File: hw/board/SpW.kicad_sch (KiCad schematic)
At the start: 8 parts

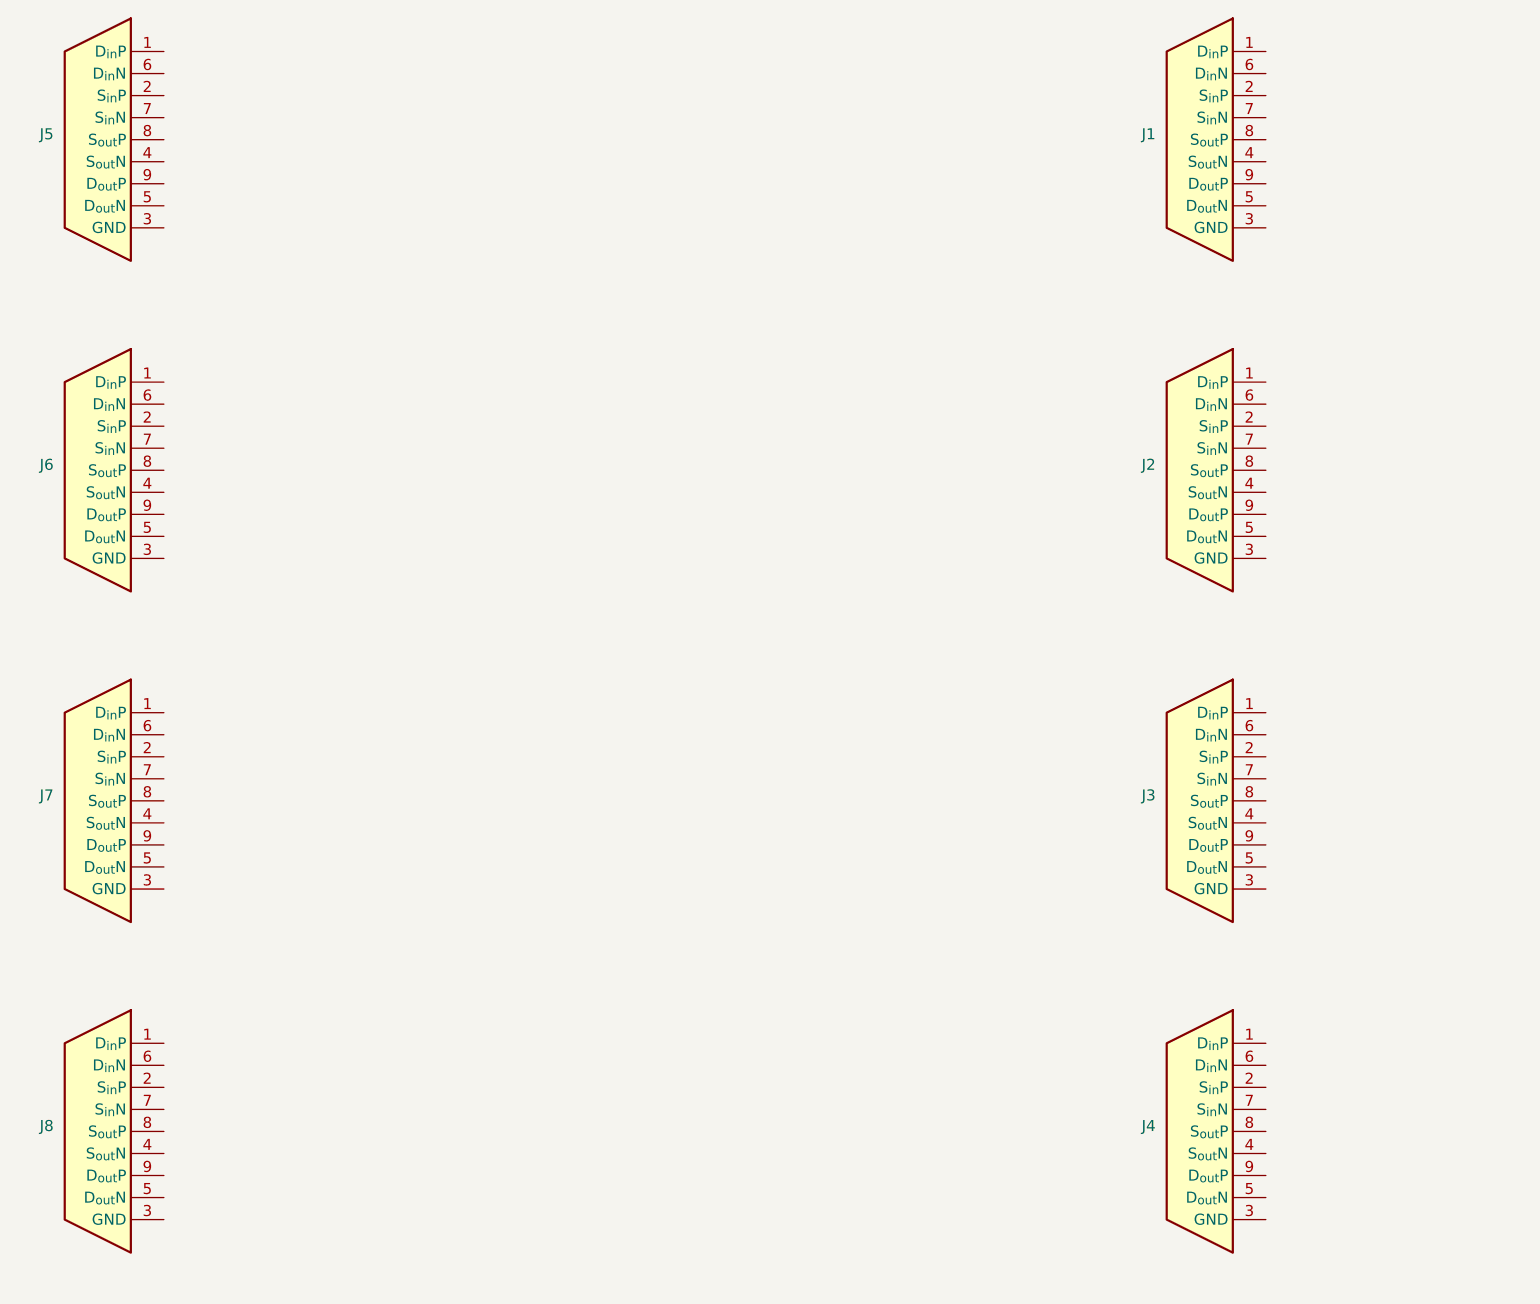
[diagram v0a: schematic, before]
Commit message: Routed DE-9 connectors
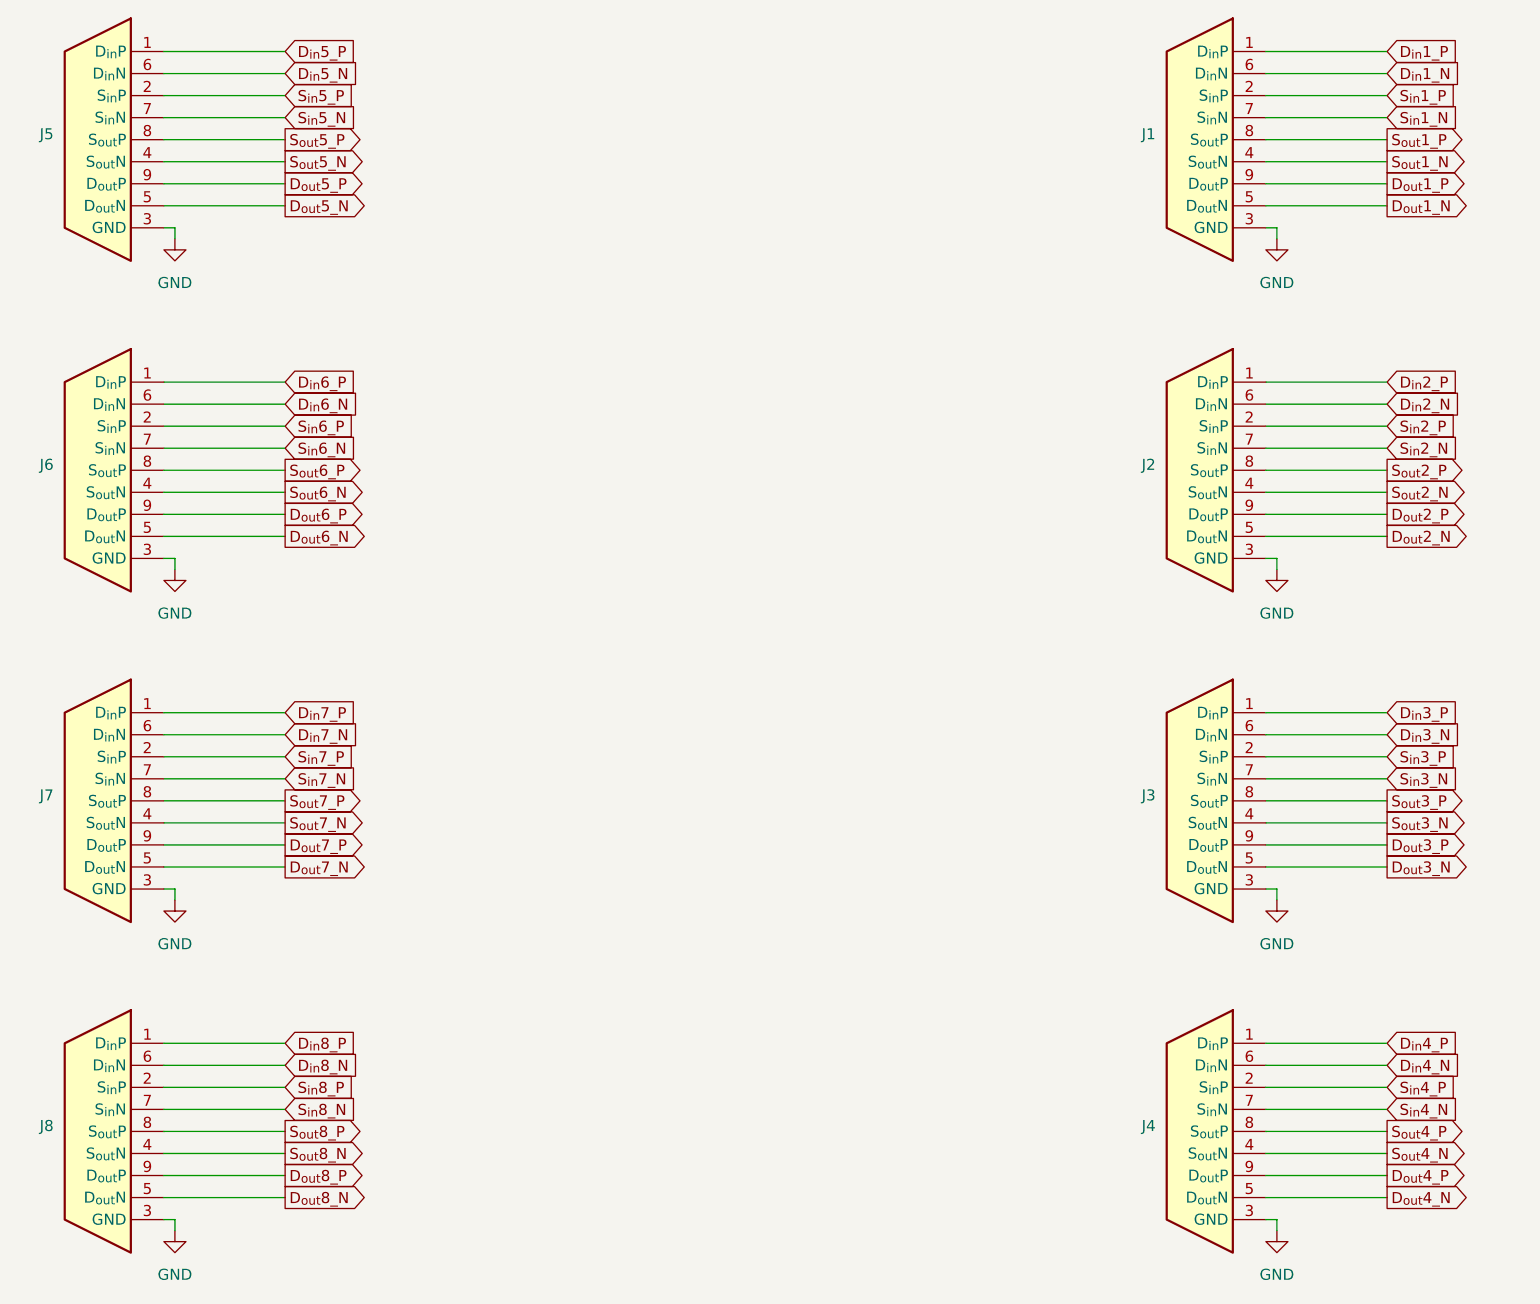
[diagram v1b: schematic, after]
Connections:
- net D_{in}3_P: now reaches J3.1 (D_{in}P)
- net S_{in}3_P: now reaches J3.2 (S_{in}P)
- net GND: now reaches J3.3 (GND)
- net GND: now also J1.3 (GND), J2.3 (GND), J4.3 (GND), J5.3 (GND), J6.3 (GND), J7.3 (GND), J8.3 (GND)
- net S_{out}3_N: now reaches J3.4 (S_{out}N)
- net D_{out}3_N: now reaches J3.5 (D_{out}N)
- net D_{in}3_N: now reaches J3.6 (D_{in}N)
- net S_{in}3_N: now reaches J3.7 (S_{in}N)
- net S_{out}3_P: now reaches J3.8 (S_{out}P)
- net D_{out}3_P: now reaches J3.9 (D_{out}P)
- net D_{in}1_P: now reaches J1.1 (D_{in}P)
- net S_{in}1_P: now reaches J1.2 (S_{in}P)
- net S_{out}1_N: now reaches J1.4 (S_{out}N)
- net D_{out}1_N: now reaches J1.5 (D_{out}N)
- net D_{in}1_N: now reaches J1.6 (D_{in}N)
- net S_{in}1_N: now reaches J1.7 (S_{in}N)
- net S_{out}1_P: now reaches J1.8 (S_{out}P)
- net D_{out}1_P: now reaches J1.9 (D_{out}P)
- net D_{in}4_P: now reaches J4.1 (D_{in}P)
- net S_{in}4_P: now reaches J4.2 (S_{in}P)
- net S_{out}4_N: now reaches J4.4 (S_{out}N)
- net D_{out}4_N: now reaches J4.5 (D_{out}N)
- net D_{in}4_N: now reaches J4.6 (D_{in}N)
- net S_{in}4_N: now reaches J4.7 (S_{in}N)
- net S_{out}4_P: now reaches J4.8 (S_{out}P)
- net D_{out}4_P: now reaches J4.9 (D_{out}P)
- net D_{in}6_P: now reaches J6.1 (D_{in}P)
- net S_{in}6_P: now reaches J6.2 (S_{in}P)
- net S_{out}6_N: now reaches J6.4 (S_{out}N)
- net D_{out}6_N: now reaches J6.5 (D_{out}N)
- net D_{in}6_N: now reaches J6.6 (D_{in}N)
- net S_{in}6_N: now reaches J6.7 (S_{in}N)
- net S_{out}6_P: now reaches J6.8 (S_{out}P)
- net D_{out}6_P: now reaches J6.9 (D_{out}P)
- net D_{in}2_P: now reaches J2.1 (D_{in}P)
- net S_{in}2_P: now reaches J2.2 (S_{in}P)
- net S_{out}2_N: now reaches J2.4 (S_{out}N)
- net D_{out}2_N: now reaches J2.5 (D_{out}N)
- net D_{in}2_N: now reaches J2.6 (D_{in}N)
- net S_{in}2_N: now reaches J2.7 (S_{in}N)
- net S_{out}2_P: now reaches J2.8 (S_{out}P)
- net D_{out}2_P: now reaches J2.9 (D_{out}P)
- net D_{in}7_P: now reaches J7.1 (D_{in}P)
- net S_{in}7_P: now reaches J7.2 (S_{in}P)
- net S_{out}7_N: now reaches J7.4 (S_{out}N)
- net D_{out}7_N: now reaches J7.5 (D_{out}N)
- net D_{in}7_N: now reaches J7.6 (D_{in}N)
- net S_{in}7_N: now reaches J7.7 (S_{in}N)
- net S_{out}7_P: now reaches J7.8 (S_{out}P)
- net D_{out}7_P: now reaches J7.9 (D_{out}P)
- net D_{in}8_P: now reaches J8.1 (D_{in}P)
- net S_{in}8_P: now reaches J8.2 (S_{in}P)
- net S_{out}8_N: now reaches J8.4 (S_{out}N)
- net D_{out}8_N: now reaches J8.5 (D_{out}N)
- net D_{in}8_N: now reaches J8.6 (D_{in}N)
- net S_{in}8_N: now reaches J8.7 (S_{in}N)
- net S_{out}8_P: now reaches J8.8 (S_{out}P)
- net D_{out}8_P: now reaches J8.9 (D_{out}P)
- net D_{in}5_P: now reaches J5.1 (D_{in}P)
- net S_{in}5_P: now reaches J5.2 (S_{in}P)
- net S_{out}5_N: now reaches J5.4 (S_{out}N)
- net D_{out}5_N: now reaches J5.5 (D_{out}N)
- net D_{in}5_N: now reaches J5.6 (D_{in}N)
- net S_{in}5_N: now reaches J5.7 (S_{in}N)
- net S_{out}5_P: now reaches J5.8 (S_{out}P)
- net D_{out}5_P: now reaches J5.9 (D_{out}P)

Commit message: Reannotated piece numbers
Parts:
- renumbered J7 to J10, J2 to J3, J3 to J4, J6 to J5, J8 to J6, J1 to J7, J4 to J8, J5 to J9
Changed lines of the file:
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@@
 		(dnp no)
 		(fields_autoplaced yes)
-		(property "Reference" "J3"
+		(property "Reference" "J4"
 			(at 151.13 111.1249 0)
 			(effects
@@
 			(project "board"
 				(path "/0e384709-6bce-4dbf-a0e0-550e970390f4/3792d272-ff69-4aa2-a357-018752cd6a75"
-					(reference "J3")
+					(reference "J4")
 					(unit 1)
 				)
@@
 		(dnp no)
 		(fields_autoplaced yes)
-		(property "Reference" "J1"
+		(property "Reference" "J7"
 			(at 151.13 34.9249 0)
 			(effects
@@
 			(project "board"
 				(path "/0e384709-6bce-4dbf-a0e0-550e970390f4/3792d272-ff69-4aa2-a357-018752cd6a75"
-					(reference "J1")
+					(reference "J7")
 					(unit 1)
 				)
@@
 		(dnp no)
 		(fields_autoplaced yes)
-		(property "Reference" "J4"
+		(property "Reference" "J8"
 			(at 151.13 149.2249 0)
 			(effects
@@
 			(project "board"
 				(path "/0e384709-6bce-4dbf-a0e0-550e970390f4/3792d272-ff69-4aa2-a357-018752cd6a75"
-					(reference "J4")
+					(reference "J8")
 					(unit 1)
 				)
@@
 		(dnp no)
 		(fields_autoplaced yes)
-		(property "Reference" "J6"
+		(property "Reference" "J5"
 			(at 24.13 73.0249 0)
 			(effects
@@
 			(project "board"
 				(path "/0e384709-6bce-4dbf-a0e0-550e970390f4/3792d272-ff69-4aa2-a357-018752cd6a75"
-					(reference "J6")
+					(reference "J5")
 					(unit 1)
 				)
@@
 		(dnp no)
 		(fields_autoplaced yes)
-		(property "Reference" "J2"
+		(property "Reference" "J3"
 			(at 151.13 73.0249 0)
 			(effects
@@
 			(project "board"
 				(path "/0e384709-6bce-4dbf-a0e0-550e970390f4/3792d272-ff69-4aa2-a357-018752cd6a75"
-					(reference "J2")
+					(reference "J3")
 					(unit 1)
 				)
@@
 		(dnp no)
 		(fields_autoplaced yes)
-		(property "Reference" "J7"
+		(property "Reference" "J10"
 			(at 24.13 111.1249 0)
 			(effects
@@
 			(project "board"
 				(path "/0e384709-6bce-4dbf-a0e0-550e970390f4/3792d272-ff69-4aa2-a357-018752cd6a75"
-					(reference "J7")
+					(reference "J10")
 					(unit 1)
 				)
@@
 		(dnp no)
 		(fields_autoplaced yes)
-		(property "Reference" "J8"
+		(property "Reference" "J6"
 			(at 24.13 149.2249 0)
 			(effects
@@
 			(project "board"
 				(path "/0e384709-6bce-4dbf-a0e0-550e970390f4/3792d272-ff69-4aa2-a357-018752cd6a75"
-					(reference "J8")
+					(reference "J6")
 					(unit 1)
 				)
@@
 		(dnp no)
 		(fields_autoplaced yes)
-		(property "Reference" "J5"
+		(property "Reference" "J9"
 			(at 24.13 34.9249 0)
 			(effects
@@
 			(project "board"
 				(path "/0e384709-6bce-4dbf-a0e0-550e970390f4/3792d272-ff69-4aa2-a357-018752cd6a75"
-					(reference "J5")
-					(unit 1)
-				)
+					(reference "J9")
+					(unit 1)
+				)
